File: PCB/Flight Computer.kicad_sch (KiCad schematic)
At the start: 0 parts

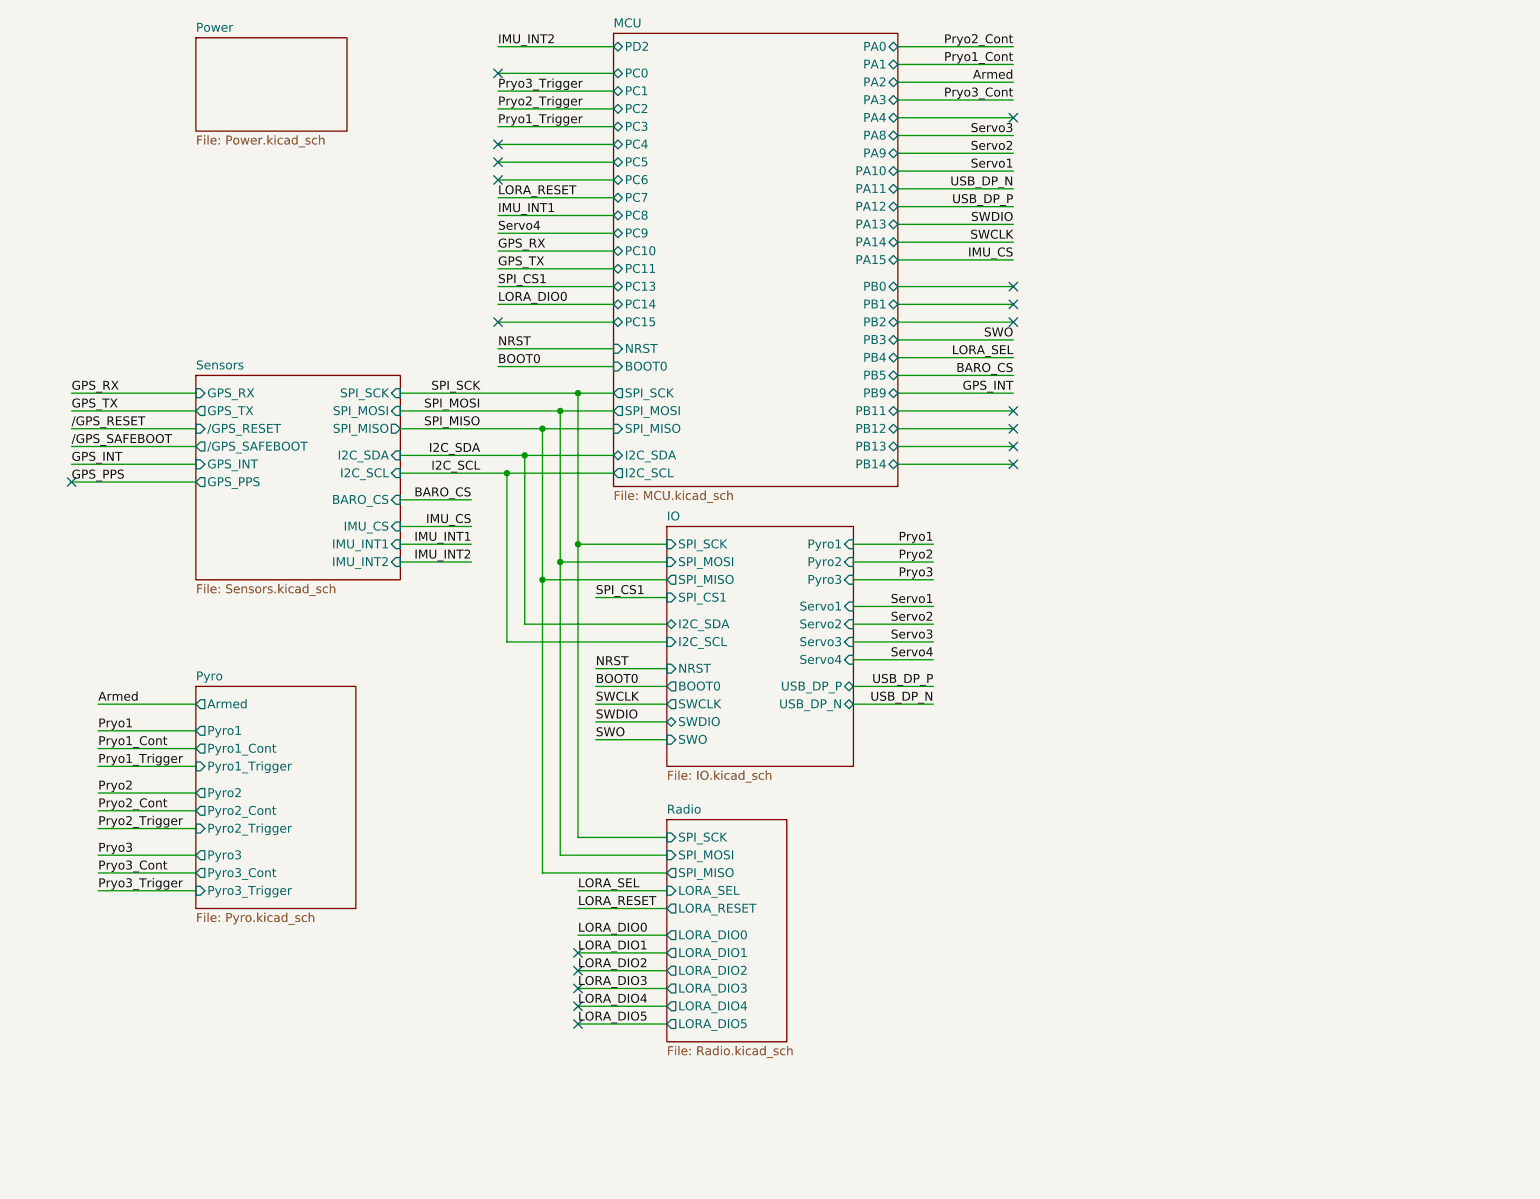
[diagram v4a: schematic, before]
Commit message: Renamed nets from pryo to pyro cause I can't spell
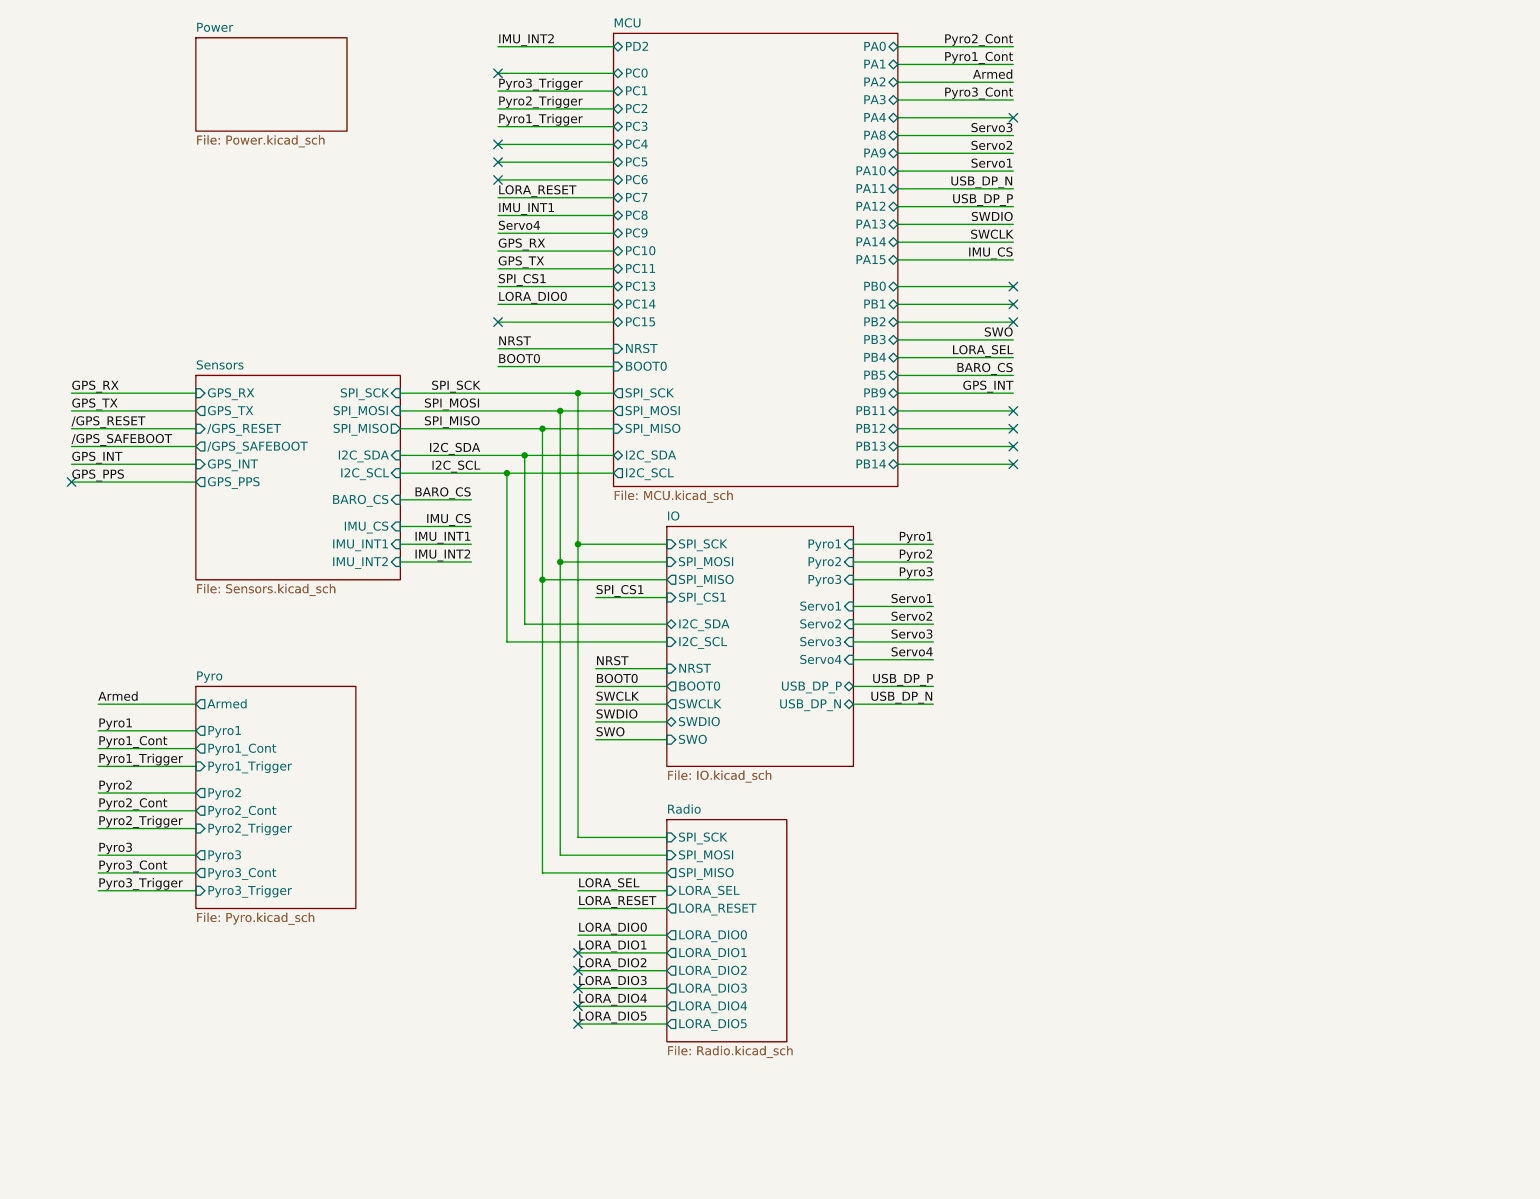
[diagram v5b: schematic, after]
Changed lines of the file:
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@@
 		)
 	)
-	(label "Pryo1_Trigger"
+	(label "Pyro1_Trigger"
 		(at 100.33 43.18 0)
 		(effects
@@
 		)
 	)
-	(label "Pryo3_Trigger"
+	(label "Pyro3_Trigger"
 		(at 100.33 38.1 0)
 		(effects
@@
 		)
 	)
-	(label "Pryo3_Trigger"
+	(label "Pyro3_Trigger"
 		(at 43.18 152.4 0)
 		(effects
@@
 		)
 	)
-	(label "Pryo1_Cont"
+	(label "Pyro1_Cont"
 		(at 173.99 34.29 180)
 		(effects
@@
 		)
 	)
-	(label "Pryo1_Cont"
+	(label "Pyro1_Cont"
 		(at 43.18 132.08 0)
 		(effects
@@
 		)
 	)
-	(label "Pryo2_Cont"
+	(label "Pyro2_Cont"
 		(at 43.18 140.97 0)
 		(effects
@@
 		)
 	)
-	(label "Pryo1_Trigger"
+	(label "Pyro1_Trigger"
 		(at 43.18 134.62 0)
 		(effects
@@
 		)
 	)
-	(label "Pryo1"
+	(label "Pyro1"
 		(at 162.56 102.87 180)
 		(effects
@@
 		)
 	)
-	(label "Pryo3_Cont"
+	(label "Pyro3_Cont"
 		(at 173.99 39.37 180)
 		(effects
@@
 		)
 	)
-	(label "Pryo2"
+	(label "Pyro2"
 		(at 162.56 105.41 180)
 		(effects
@@
 		)
 	)
-	(label "Pryo3_Cont"
+	(label "Pyro3_Cont"
 		(at 43.18 149.86 0)
 		(effects
@@
 		)
 	)
-	(label "Pryo3"
+	(label "Pyro3"
 		(at 43.18 147.32 0)
 		(effects
@@
 		)
 	)
-	(label "Pryo3"
+	(label "Pyro3"
 		(at 162.56 107.95 180)
 		(effects
@@
 		)
 	)
-	(label "Pryo2_Trigger"
+	(label "Pyro2_Trigger"
 		(at 100.33 40.64 0)
 		(effects
@@
 		)
 	)
-	(label "Pryo2_Cont"
+	(label "Pyro2_Cont"
 		(at 173.99 31.75 180)
 		(effects
@@
 		)
 	)
-	(label "Pryo2_Trigger"
+	(label "Pyro2_Trigger"
 		(at 43.18 143.51 0)
 		(effects
@@
 		)
 	)
-	(label "Pryo1"
+	(label "Pyro1"
 		(at 43.18 129.54 0)
 		(effects
@@
 		)
 	)
-	(label "Pryo2"
+	(label "Pyro2"
 		(at 43.18 138.43 0)
 		(effects

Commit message: Cleaned up schematic Change from SPI and I2C to busses
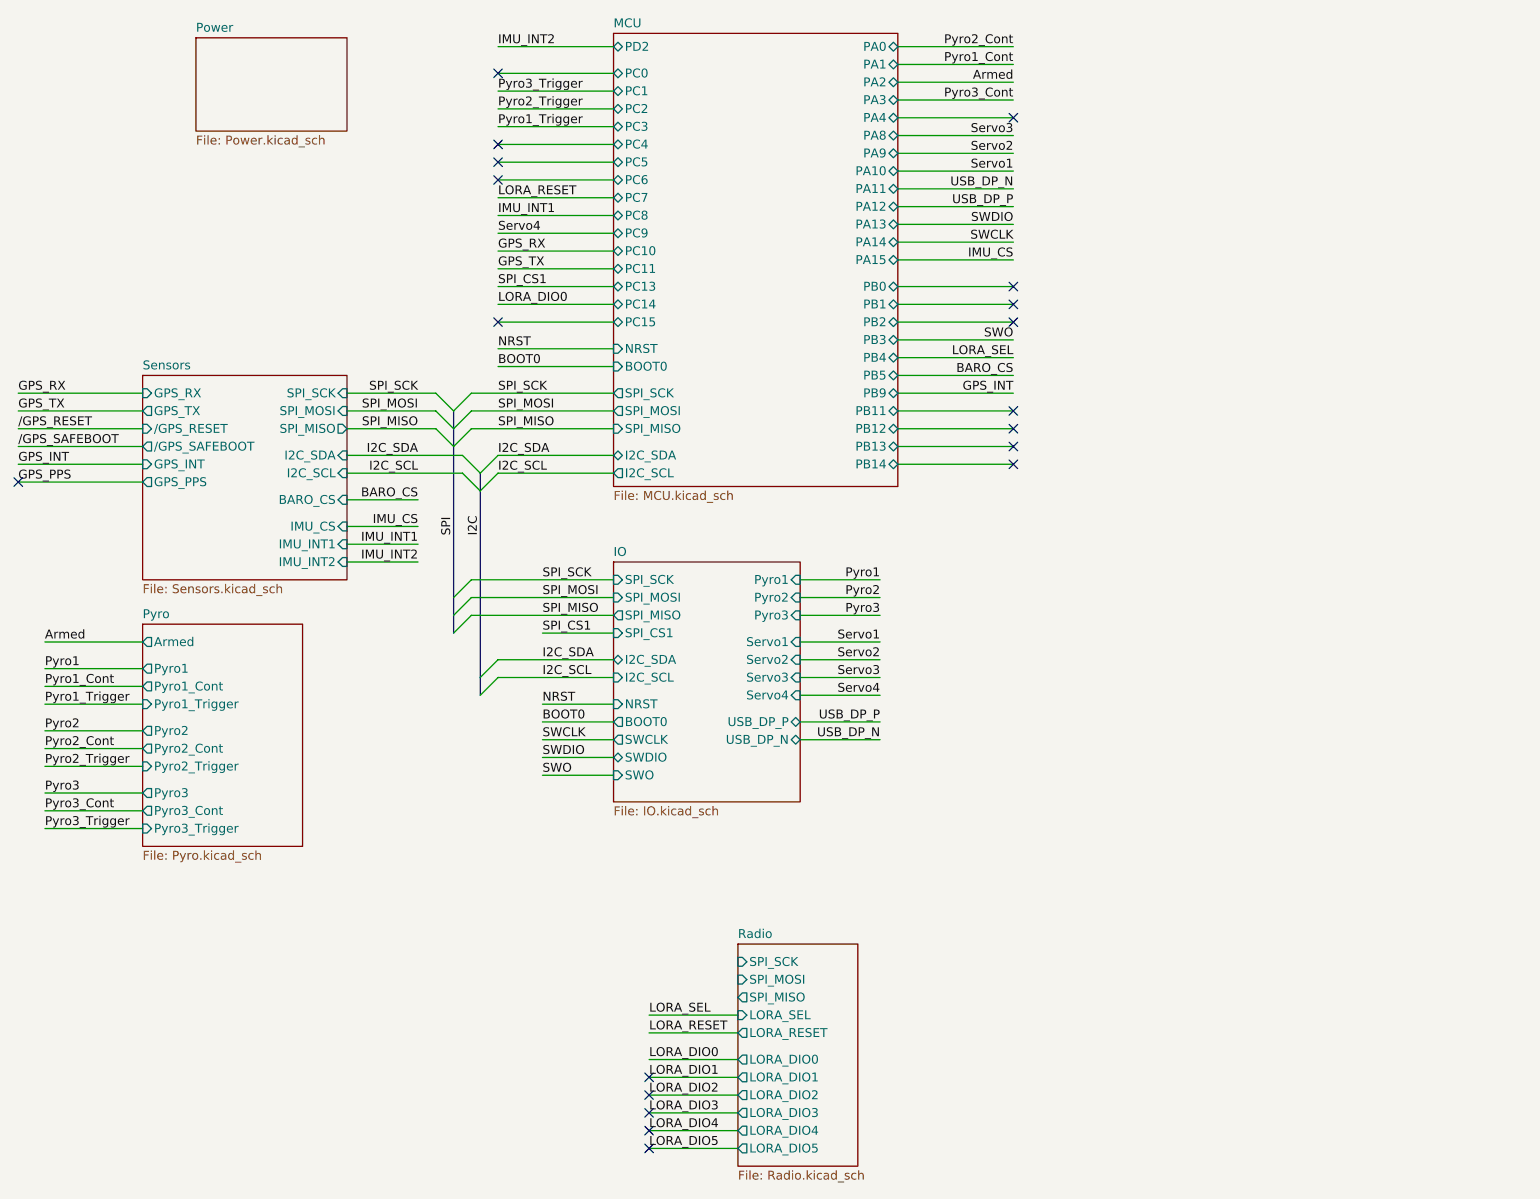
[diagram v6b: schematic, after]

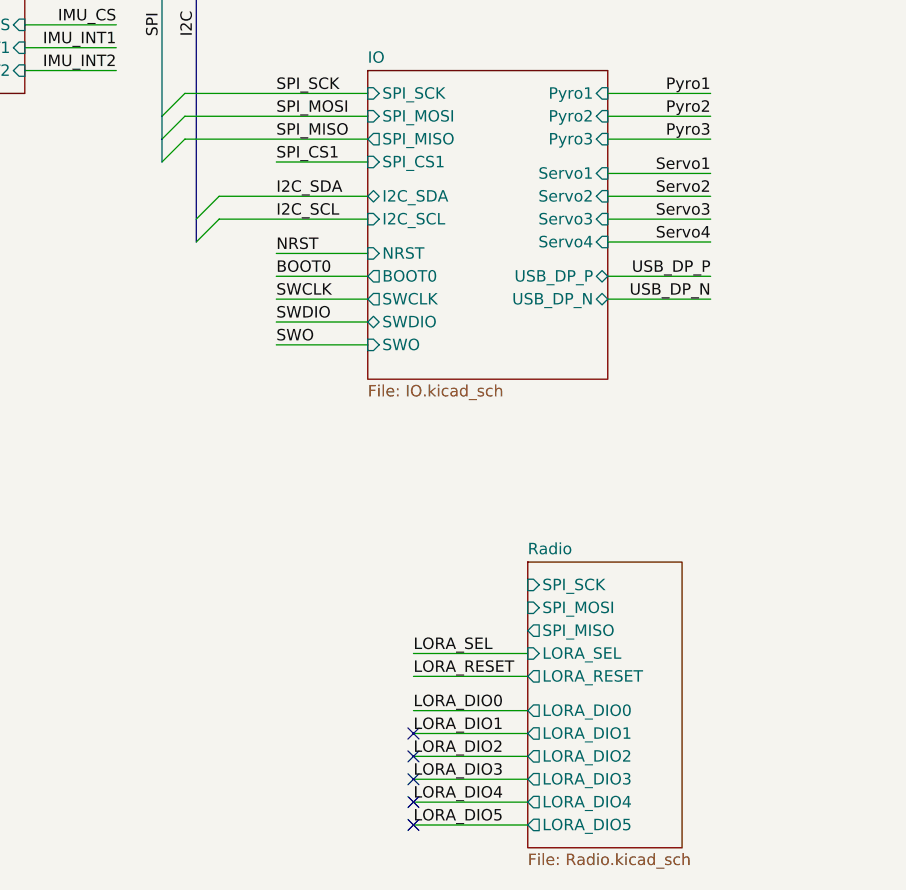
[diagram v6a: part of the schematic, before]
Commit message: Update Barometer SPI connection
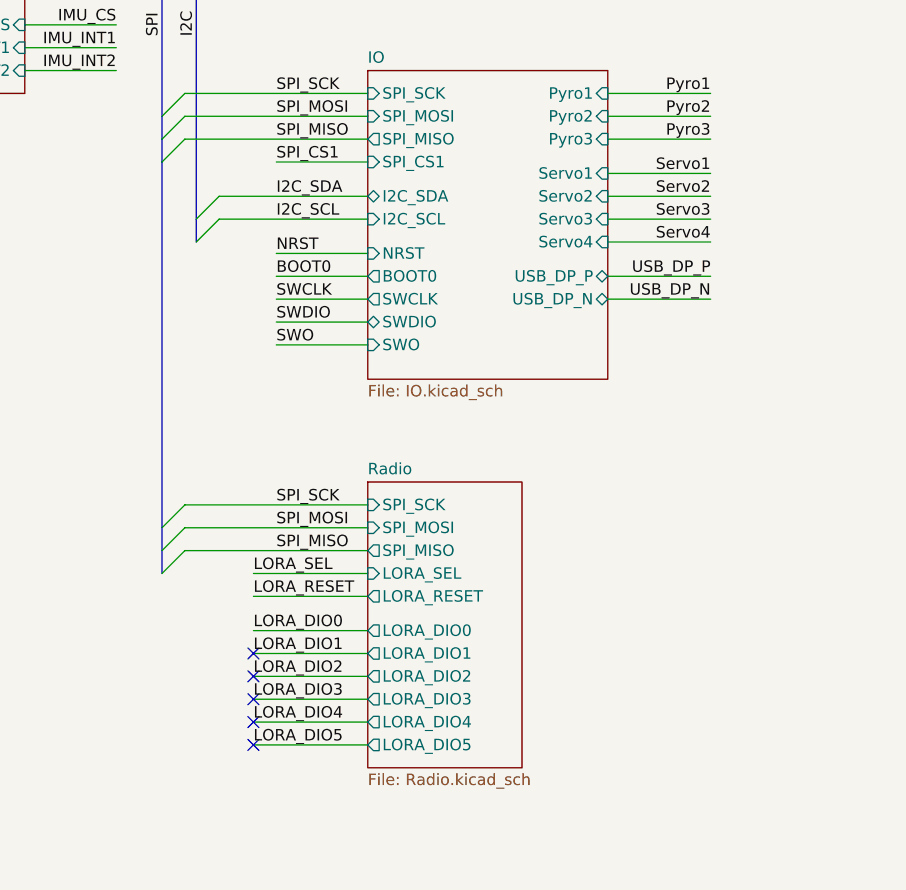
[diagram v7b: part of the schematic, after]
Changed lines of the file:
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@@
 	)
 	(no_connect
-		(at 121.92 179.07)
+		(at 104.14 170.18)
 	)
 	(no_connect
@@
 	)
 	(no_connect
-		(at 121.92 181.61)
+		(at 104.14 172.72)
 	)
 	(no_connect
@@
 	)
 	(no_connect
-		(at 121.92 186.69)
+		(at 104.14 177.8)
 	)
 	(no_connect
-		(at 121.92 189.23)
+		(at 104.14 180.34)
 	)
 	(no_connect
@@
 	)
 	(no_connect
-		(at 121.92 184.15)
+		(at 104.14 175.26)
 	)
 	(no_connect
@@
 	)
 	(bus_entry
+		(at 93.98 161.29)
+		(size 2.54 -2.54)
+		(stroke
+			(width 0)
+			(type default)
+		)
+	)
+	(bus_entry
 		(at 93.98 86.36)
 		(size 2.54 -2.54)
@@
 	)
 	(bus_entry
+		(at 93.98 158.75)
+		(size 2.54 -2.54)
+		(stroke
+			(width 0)
+			(type default)
+		)
+	)
+	(bus_entry
 		(at 93.98 110.49)
 		(size 2.54 -2.54)
@@
 	)
 	(bus_entry
+		(at 93.98 156.21)
+		(size 2.54 -2.54)
+		(stroke
+			(width 0)
+			(type default)
+		)
+	)
+	(bus_entry
 		(at 91.44 81.28)
 		(size 2.54 2.54)
@@
 	(wire
 		(pts
-			(xy 121.92 189.23) (xy 134.62 189.23)
+			(xy 104.14 180.34) (xy 116.84 180.34)
 		)
 		(stroke
@@
 		)
 	)
+	(bus
+		(pts
+			(xy 93.98 158.75) (xy 93.98 161.29)
+		)
+		(stroke
+			(width 0)
+			(type default)
+		)
+	)
 	(wire
 		(pts
@@
 	(wire
 		(pts
-			(xy 121.92 184.15) (xy 134.62 184.15)
+			(xy 104.14 175.26) (xy 116.84 175.26)
 		)
 		(stroke
@@
 	(wire
 		(pts
-			(xy 121.92 181.61) (xy 134.62 181.61)
+			(xy 104.14 172.72) (xy 116.84 172.72)
 		)
 		(stroke
@@
 	(wire
 		(pts
+			(xy 96.52 156.21) (xy 116.84 156.21)
+		)
+		(stroke
+			(width 0)
+			(type default)
+		)
+	)
+	(wire
+		(pts
 			(xy 100.33 50.8) (xy 116.84 50.8)
 		)
@@
 	(wire
 		(pts
-			(xy 121.92 186.69) (xy 134.62 186.69)
+			(xy 104.14 177.8) (xy 116.84 177.8)
 		)
 		(stroke
@@
 	(wire
 		(pts
-			(xy 121.92 170.18) (xy 134.62 170.18)
+			(xy 104.14 161.29) (xy 116.84 161.29)
 		)
 		(stroke
@@
 	(wire
 		(pts
-			(xy 121.92 179.07) (xy 134.62 179.07)
+			(xy 104.14 170.18) (xy 116.84 170.18)
 		)
 		(stroke
@@
 	(wire
 		(pts
+			(xy 96.52 153.67) (xy 116.84 153.67)
+		)
+		(stroke
+			(width 0)
+			(type default)
+		)
+	)
+	(wire
+		(pts
 			(xy 100.33 45.72) (xy 116.84 45.72)
 		)
@@
 		)
 	)
+	(bus
+		(pts
+			(xy 93.98 156.21) (xy 93.98 158.75)
+		)
+		(stroke
+			(width 0)
+			(type default)
+		)
+	)
+	(bus
+		(pts
+			(xy 93.98 115.57) (xy 93.98 156.21)
+		)
+		(stroke
+			(width 0)
+			(type default)
+		)
+	)
 	(wire
 		(pts
@@
 	(wire
 		(pts
-			(xy 121.92 172.72) (xy 134.62 172.72)
+			(xy 104.14 163.83) (xy 116.84 163.83)
 		)
 		(stroke
@@
 	(wire
 		(pts
-			(xy 121.92 176.53) (xy 134.62 176.53)
+			(xy 104.14 167.64) (xy 116.84 167.64)
 		)
 		(stroke
@@
 		(pts
 			(xy 157.48 88.9) (xy 173.99 88.9)
+		)
+		(stroke
+			(width 0)
+			(type default)
+		)
+	)
+	(wire
+		(pts
+			(xy 96.52 158.75) (xy 116.84 158.75)
 		)
 		(stroke
@@
 	)
 	(label "LORA_DIO4"
-		(at 121.92 186.69 0)
+		(at 104.14 177.8 0)
 		(effects
 			(font
@@
 		)
 	)
+	(label "SPI_SCK"
+		(at 106.68 153.67 0)
+		(effects
+			(font
+				(size 1.27 1.27)
+			)
+			(justify left bottom)
+		)
+	)
 	(label "IMU_INT1"
 		(at 100.33 55.88 0)
@@
 	)
 	(label "LORA_RESET"
-		(at 121.92 172.72 0)
+		(at 104.14 163.83 0)
 		(effects
 			(font
@@
 	)
 	(label "LORA_DIO1"
-		(at 121.92 179.07 0)
+		(at 104.14 170.18 0)
 		(effects
 			(font
@@
 		)
 	)
+	(label "SPI_MISO"
+		(at 106.68 158.75 0)
+		(effects
+			(font
+				(size 1.27 1.27)
+			)
+			(justify left bottom)
+		)
+	)
 	(label "SPI"
 		(at 93.98 101.6 90)
@@
 	)
 	(label "LORA_DIO2"
-		(at 121.92 181.61 0)
+		(at 104.14 172.72 0)
 		(effects
 			(font
@@
 	)
 	(label "LORA_DIO5"
-		(at 121.92 189.23 0)
+		(at 104.14 180.34 0)
 		(effects
 			(font
@@
 	)
 	(label "LORA_DIO3"
-		(at 121.92 184.15 0)
+		(at 104.14 175.26 0)
+		(effects
+			(font
+				(size 1.27 1.27)
+			)
+			(justify left bottom)
+		)
+	)
+	(label "SPI_MOSI"
+		(at 106.68 156.21 0)
 		(effects
 			(font
@@
 	)
 	(label "LORA_DIO0"
-		(at 121.92 176.53 0)
+		(at 104.14 167.64 0)
 		(effects
 			(font
@@
 	)
 	(label "LORA_SEL"
-		(at 121.92 170.18 0)
+		(at 104.14 161.29 0)
 		(effects
 			(font
@@
 	)
 	(sheet
-		(at 134.62 160.02)
+		(at 116.84 151.13)
 		(size 17.145 31.75)
 		(exclude_from_sim no)
@@
 		)
 		(property "Sheetname" "Radio"
-			(at 134.62 159.3084 0)
+			(at 116.84 150.4184 0)
 			(effects
 				(font
@@
 		)
 		(property "Sheetfile" "Radio.kicad_sch"
-			(at 134.62 192.3546 0)
+			(at 116.84 183.4646 0)
 			(effects
 				(font
@@
 		)
 		(pin "SPI_SCK" input
-			(at 134.62 162.56 180)
+			(at 116.84 153.67 180)
 			(effects
 				(font
@@
 		)
 		(pin "SPI_MOSI" input
-			(at 134.62 165.1 180)
+			(at 116.84 156.21 180)
 			(effects
 				(font
@@
 		)
 		(pin "SPI_MISO" output
-			(at 134.62 167.64 180)
+			(at 116.84 158.75 180)
 			(effects
 				(font
@@
 		)
 		(pin "LORA_SEL" input
-			(at 134.62 170.18 180)
+			(at 116.84 161.29 180)
 			(effects
 				(font
@@
 		)
 		(pin "LORA_DIO1" output
-			(at 134.62 179.07 180)
+			(at 116.84 170.18 180)
 			(effects
 				(font
@@
 		)
 		(pin "LORA_RESET" output
-			(at 134.62 172.72 180)
+			(at 116.84 163.83 180)
 			(effects
 				(font
@@
 		)
 		(pin "LORA_DIO4" output
-			(at 134.62 186.69 180)
+			(at 116.84 177.8 180)
 			(effects
 				(font
@@
 		)
 		(pin "LORA_DIO2" output
-			(at 134.62 181.61 180)
+			(at 116.84 172.72 180)
 			(effects
 				(font
@@
 		)
 		(pin "LORA_DIO5" output
-			(at 134.62 189.23 180)
+			(at 116.84 180.34 180)
 			(effects
 				(font
@@
 		)
 		(pin "LORA_DIO0" output
-			(at 134.62 176.53 180)
+			(at 116.84 167.64 180)
 			(effects
 				(font
@@
 		)
 		(pin "LORA_DIO3" output
-			(at 134.62 184.15 180)
-			(effects
-				(font
+			(at 116.84 175.26 180)
+			(effects
+				(font
